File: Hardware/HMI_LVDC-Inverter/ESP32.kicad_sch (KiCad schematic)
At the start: 36 parts, among them U2 ESP32-WROOM-32E-N16, Y2 32.768KHz

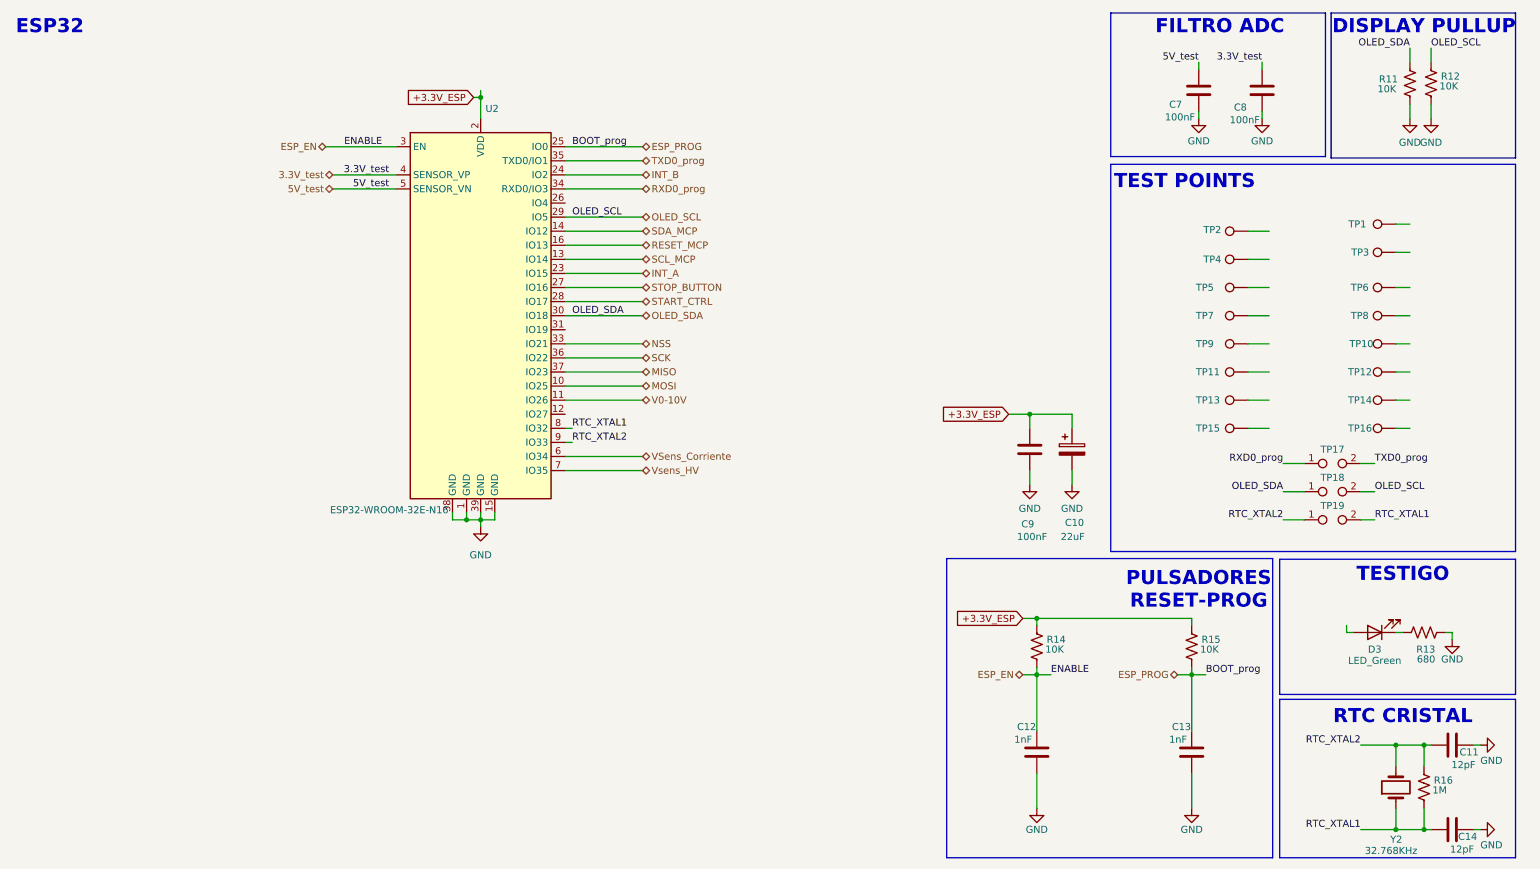
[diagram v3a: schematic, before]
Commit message: Falta resolver los pulsadores
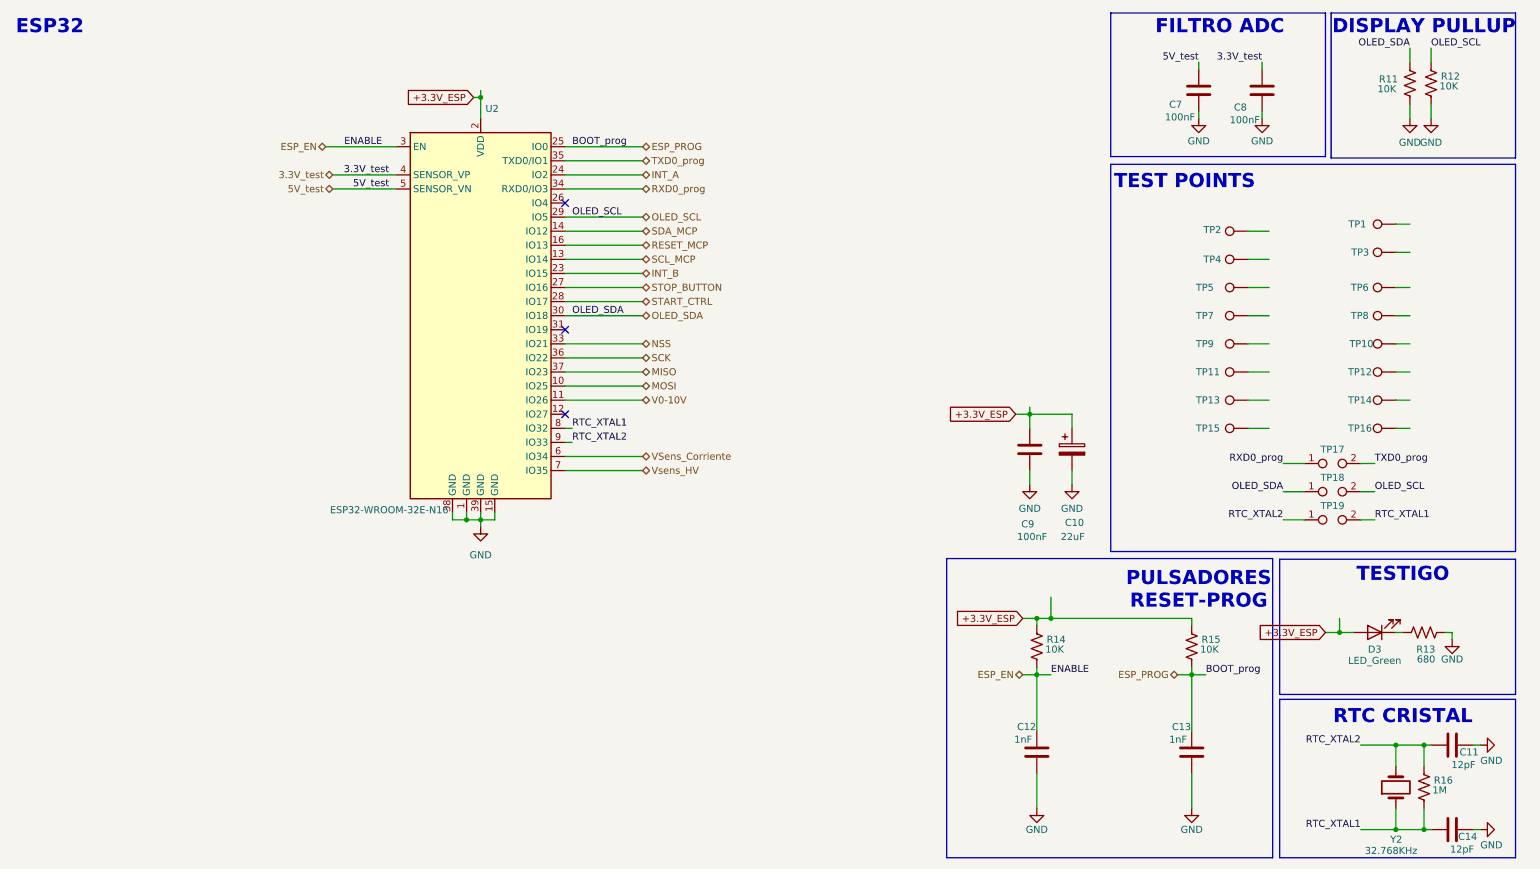
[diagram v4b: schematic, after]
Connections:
- net +3.3V_ESP: now also D3.2 (A)
- net INT_A: now also U2.24 (IO2); no longer U2.23 (IO15)
- net INT_B: now also U2.23 (IO15); no longer U2.24 (IO2)
- no-connect marks 0 -> 3

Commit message: Agregado y corrección de borneras
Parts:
- removed TP17, TP18, TP19: TestPoint_2Pole, symbol Connector:TestPoint_2Pole
- TP1, TP10, TP11, TP12, TP13, TP14, TP15, TP16, TP2, TP3, TP4, TP5, TP6, TP7, TP8, TP9: footprint Connector_Pin:Pin_D0.7mm_L6.5mm_W1.8mm_FlatFork -> TestPoint:TestPoint_Pad_D1.0mm
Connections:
- net OLED_SCL: now also TP16.1
- net OLED_SDA: now also TP15.1

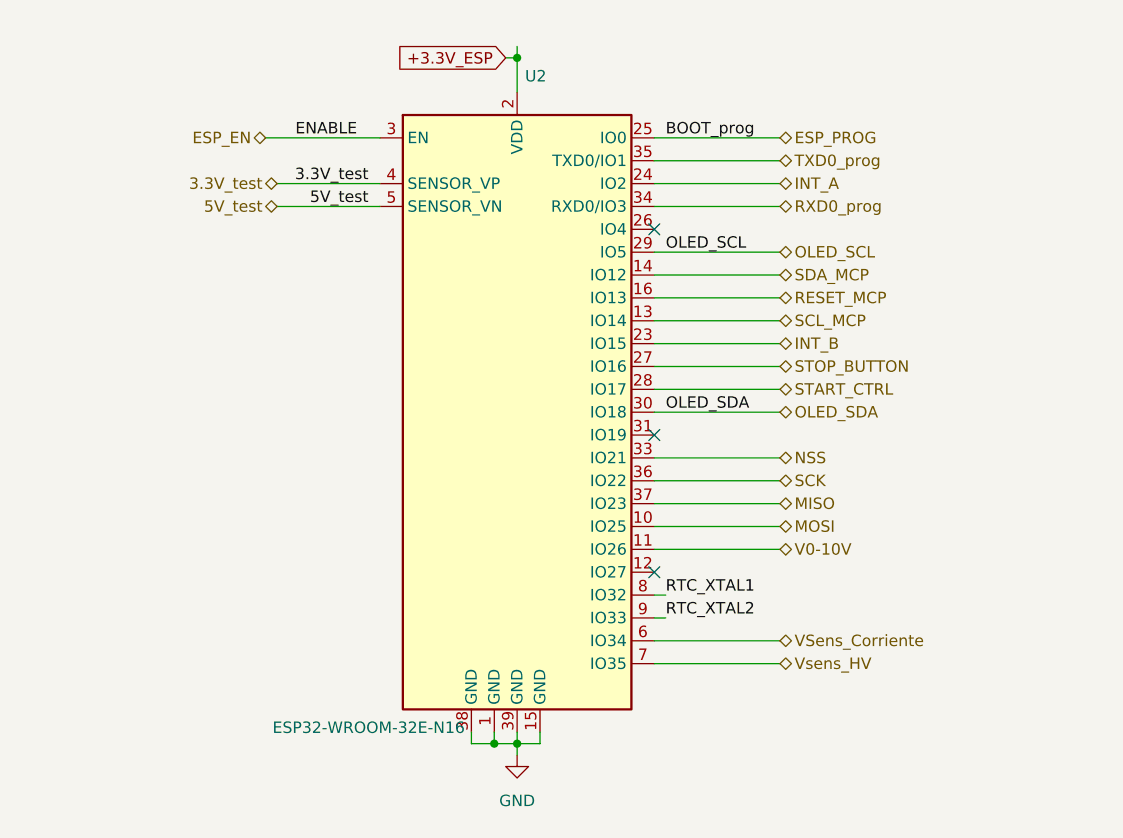
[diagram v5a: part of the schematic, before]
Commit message: Terminada la placa del HMI con revisión de reglas de diseño
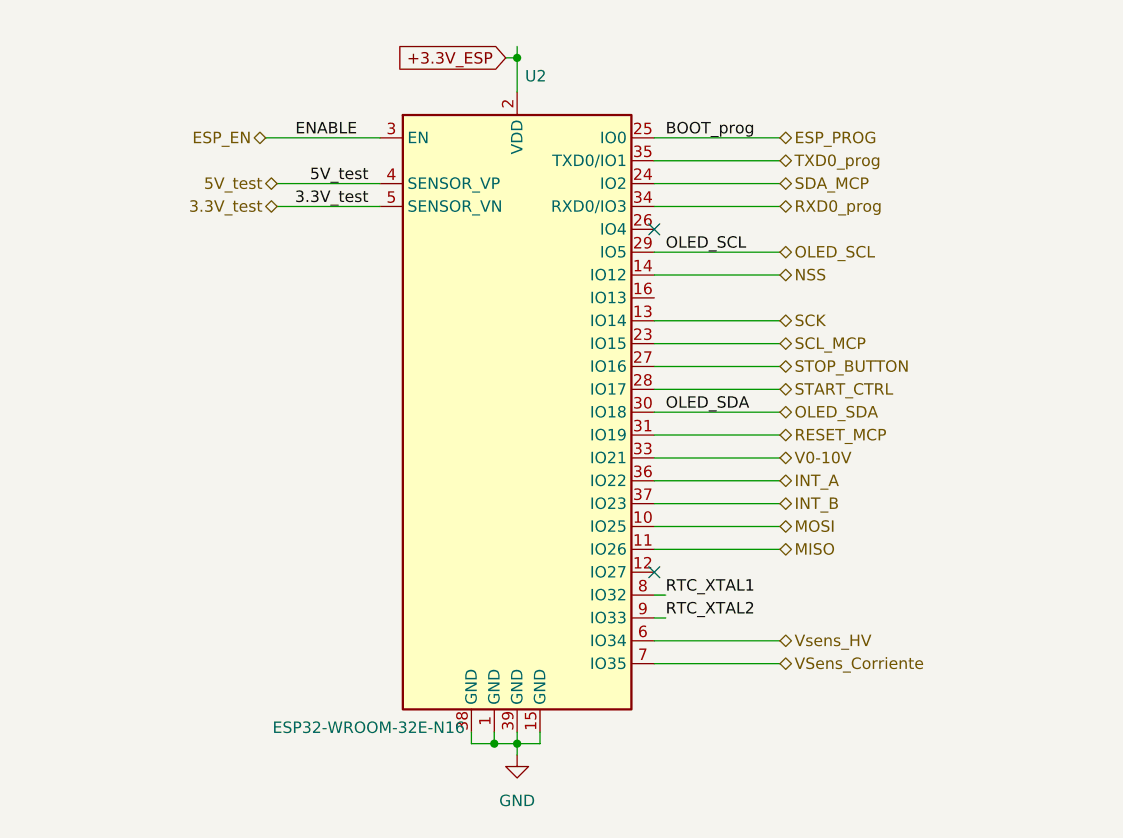
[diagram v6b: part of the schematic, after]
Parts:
- U2: footprint RF_Module:ESP32-WROOM-32D -> RF_Module:ESP32-WROOM-32E
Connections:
- net 3.3V_test: now also U2.5 (SENSOR_VN); no longer U2.4 (SENSOR_VP)
- net 5V_test: now also U2.4 (SENSOR_VP); no longer U2.5 (SENSOR_VN)
- net INT_A: now also U2.36 (IO22); no longer U2.24 (IO2)
- net INT_B: now also U2.37 (IO23); no longer U2.23 (IO15)
- net MISO: now also U2.11 (IO26); no longer U2.37 (IO23)
- net NSS: now also U2.14 (IO12); no longer U2.33 (IO21)
- net RESET_MCP: now also U2.31 (IO19); no longer U2.16 (IO13)
- net SCK: now also U2.13 (IO14); no longer U2.36 (IO22)
- net SCL_MCP: now also U2.23 (IO15); no longer U2.13 (IO14)
- net SDA_MCP: now also U2.24 (IO2); no longer U2.14 (IO12)
- net V0-10V: now also U2.33 (IO21); no longer U2.11 (IO26)
- net VSens_Corriente: now also U2.7 (IO35); no longer U2.6 (IO34)
- net Vsens_HV: now also U2.6 (IO34); no longer U2.7 (IO35)
- no-connect marks 3 -> 2
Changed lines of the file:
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@@
 	)
 	(no_connect
-		(at 111.76 69.85)
-	)
-	(no_connect
 		(at 111.76 46.99)
 	)
@@
 	(wire
 		(pts
-			(xy 125.73 74.93) (xy 111.76 74.93)
+			(xy 238.76 87.63) (xy 234.95 87.63)
 		)
 		(stroke
@@
 	(wire
 		(pts
-			(xy 238.76 87.63) (xy 234.95 87.63)
+			(xy 125.73 72.39) (xy 111.76 72.39)
 		)
 		(stroke
@@
 	(wire
 		(pts
-			(xy 125.73 77.47) (xy 111.76 77.47)
+			(xy 111.76 92.71) (xy 125.73 92.71)
 		)
 		(stroke
@@
 	(wire
 		(pts
-			(xy 125.73 52.07) (xy 111.76 52.07)
+			(xy 125.73 77.47) (xy 111.76 77.47)
 		)
 		(stroke
@@
 	(wire
 		(pts
-			(xy 125.73 54.61) (xy 111.76 54.61)
+			(xy 69.85 41.91) (xy 81.28 41.91)
 		)
 		(stroke
@@
 	(wire
 		(pts
-			(xy 125.73 41.91) (xy 111.76 41.91)
+			(xy 261.62 144.78) (xy 266.7 144.78)
 		)
 		(stroke
@@
 	(wire
 		(pts
-			(xy 261.62 144.78) (xy 266.7 144.78)
+			(xy 111.76 82.55) (xy 125.73 82.55)
 		)
 		(stroke
@@
 	(wire
 		(pts
-			(xy 111.76 67.31) (xy 125.73 67.31)
+			(xy 125.73 74.93) (xy 111.76 74.93)
 		)
 		(stroke
@@
 	(wire
 		(pts
-			(xy 264.16 62.23) (xy 261.62 62.23)
+			(xy 111.76 67.31) (xy 125.73 67.31)
 		)
 		(stroke
@@
 	(wire
 		(pts
-			(xy 125.73 80.01) (xy 111.76 80.01)
+			(xy 264.16 62.23) (xy 261.62 62.23)
 		)
 		(stroke
@@
 	(wire
 		(pts
-			(xy 224.79 149.86) (xy 224.79 156.21)
+			(xy 125.73 80.01) (xy 111.76 80.01)
 		)
 		(stroke
@@
 	(wire
 		(pts
-			(xy 238.76 82.55) (xy 234.95 82.55)
+			(xy 224.79 149.86) (xy 224.79 156.21)
 		)
 		(stroke
@@
 	(wire
 		(pts
-			(xy 266.7 144.78) (xy 266.7 148.59)
+			(xy 238.76 82.55) (xy 234.95 82.55)
 		)
 		(stroke
@@
 	(wire
 		(pts
-			(xy 111.76 49.53) (xy 125.73 49.53)
+			(xy 266.7 144.78) (xy 266.7 148.59)
 		)
 		(stroke
@@
 	(wire
 		(pts
-			(xy 125.73 95.25) (xy 111.76 95.25)
+			(xy 111.76 49.53) (xy 125.73 49.53)
 		)
 		(stroke
@@
 	(wire
 		(pts
-			(xy 69.85 44.45) (xy 81.28 44.45)
-		)
-		(stroke
-			(width 0)
-			(type default)
-		)
-	)
-	(wire
-		(pts
 			(xy 255.27 160.02) (xy 261.62 160.02)
 		)
@@
 	(wire
 		(pts
-			(xy 125.73 59.69) (xy 111.76 59.69)
+			(xy 125.73 69.85) (xy 111.76 69.85)
 		)
 		(stroke
@@
 	(wire
 		(pts
-			(xy 125.73 82.55) (xy 111.76 82.55)
-		)
-		(stroke
-			(width 0)
-			(type default)
-		)
-	)
-	(wire
-		(pts
 			(xy 226.06 31.75) (xy 226.06 30.48)
 		)
@@
 	(wire
 		(pts
-			(xy 195.58 85.09) (xy 203.2 85.09)
+			(xy 125.73 59.69) (xy 111.76 59.69)
 		)
 		(stroke
@@
 	(wire
 		(pts
-			(xy 203.2 95.25) (xy 203.2 97.79)
+			(xy 125.73 41.91) (xy 111.76 41.91)
 		)
 		(stroke
@@
 	(wire
 		(pts
-			(xy 261.62 156.21) (xy 261.62 160.02)
+			(xy 195.58 85.09) (xy 203.2 85.09)
 		)
 		(stroke
@@
 	(wire
 		(pts
-			(xy 238.76 72.39) (xy 234.95 72.39)
+			(xy 203.2 95.25) (xy 203.2 97.79)
 		)
 		(stroke
@@
 	(wire
 		(pts
-			(xy 248.92 124.46) (xy 251.46 124.46)
+			(xy 261.62 156.21) (xy 261.62 160.02)
 		)
 		(stroke
@@
 	(wire
 		(pts
-			(xy 125.73 57.15) (xy 111.76 57.15)
+			(xy 238.76 72.39) (xy 234.95 72.39)
 		)
 		(stroke
@@
 	(wire
 		(pts
-			(xy 96.52 26.67) (xy 96.52 27.94)
+			(xy 248.92 124.46) (xy 251.46 124.46)
 		)
 		(stroke
@@
 	(wire
 		(pts
-			(xy 224.79 132.08) (xy 224.79 142.24)
+			(xy 96.52 26.67) (xy 96.52 27.94)
 		)
 		(stroke
@@
 	(wire
 		(pts
-			(xy 125.73 92.71) (xy 111.76 92.71)
+			(xy 224.79 132.08) (xy 224.79 142.24)
 		)
 		(stroke
@@
 	(wire
 		(pts
-			(xy 125.73 72.39) (xy 111.76 72.39)
+			(xy 238.76 67.31) (xy 234.95 67.31)
 		)
 		(stroke
@@
 	(wire
 		(pts
-			(xy 238.76 67.31) (xy 234.95 67.31)
+			(xy 196.85 121.92) (xy 196.85 123.19)
 		)
 		(stroke
@@
 	(wire
 		(pts
-			(xy 196.85 121.92) (xy 196.85 123.19)
+			(xy 264.16 31.75) (xy 264.16 29.21)
 		)
 		(stroke
@@
 	(wire
 		(pts
-			(xy 264.16 31.75) (xy 264.16 29.21)
+			(xy 264.16 72.39) (xy 261.62 72.39)
 		)
 		(stroke
@@
 	(wire
 		(pts
-			(xy 264.16 72.39) (xy 261.62 72.39)
+			(xy 111.76 95.25) (xy 125.73 95.25)
+		)
+		(stroke
+			(width 0)
+			(type default)
+		)
+	)
+	(wire
+		(pts
+			(xy 111.76 57.15) (xy 125.73 57.15)
 		)
 		(stroke
@@
 	(wire
 		(pts
-			(xy 69.85 41.91) (xy 81.28 41.91)
+			(xy 111.76 52.07) (xy 125.73 52.07)
+		)
+		(stroke
+			(width 0)
+			(type default)
+		)
+	)
+	(wire
+		(pts
+			(xy 69.85 44.45) (xy 81.28 44.45)
 		)
 		(stroke
@@
 		)
 	)
-	(label "5V_test"
-		(at 80.01 44.45 180)
-		(effects
-			(font
-				(size 1.27 1.27)
-			)
-			(justify right bottom)
-		)
-	)
 	(label "OLED_SDA"
 		(at 238.76 87.63 0)
@@
 		)
 	)
+	(label "5V_test"
+		(at 80.01 41.91 180)
+		(effects
+			(font
+				(size 1.27 1.27)
+			)
+			(justify right bottom)
+		)
+	)
 	(label "ENABLE"
 		(at 199.39 132.08 0)
@@
 	)
 	(label "3.3V_test"
-		(at 80.01 41.91 180)
+		(at 80.01 44.45 180)
 		(effects
 			(font
@@
 	(hierarchical_label "SCL_MCP"
 		(shape bidirectional)
-		(at 125.73 57.15 0)
+		(at 125.73 59.69 0)
 		(effects
 			(font
@@
 	(hierarchical_label "INT_A"
 		(shape bidirectional)
-		(at 125.73 41.91 0)
+		(at 125.73 74.93 0)
 		(effects
 			(font
@@
 	(hierarchical_label "V0-10V"
 		(shape bidirectional)
-		(at 125.73 82.55 0)
+		(at 125.73 72.39 0)
 		(effects
 			(font
@@
 		)
 	)
+	(hierarchical_label "5V_test"
+		(shape bidirectional)
+		(at 69.85 41.91 180)
+		(effects
+			(font
+				(size 1.27 1.27)
+			)
+			(justify right)
+		)
+	)
 	(hierarchical_label "RESET_MCP"
 		(shape bidirectional)
-		(at 125.73 54.61 0)
+		(at 125.73 69.85 0)
 		(effects
 			(font
@@
 	(hierarchical_label "NSS"
 		(shape bidirectional)
-		(at 125.73 72.39 0)
+		(at 125.73 52.07 0)
 		(effects
 			(font
@@
 	(hierarchical_label "VSens_Corriente"
 		(shape bidirectional)
-		(at 125.73 92.71 0)
+		(at 125.73 95.25 0)
 		(effects
 			(font
@@
 		)
 	)
-	(hierarchical_label "5V_test"
-		(shape bidirectional)
-		(at 69.85 44.45 180)
-		(effects
-			(font
-				(size 1.27 1.27)
-			)
-			(justify right)
-		)
-	)
 	(hierarchical_label "ESP_PROG"
 		(shape bidirectional)
@@
 	(hierarchical_label "MISO"
 		(shape bidirectional)
-		(at 125.73 77.47 0)
+		(at 125.73 82.55 0)
 		(effects
 			(font
@@
 	(hierarchical_label "SCK"
 		(shape bidirectional)
-		(at 125.73 74.93 0)
+		(at 125.73 57.15 0)
 		(effects
 			(font
@@
 	(hierarchical_label "Vsens_HV"
 		(shape bidirectional)
-		(at 125.73 95.25 0)
+		(at 125.73 92.71 0)
 		(effects
 			(font
@@
 	(hierarchical_label "INT_B"
 		(shape bidirectional)
-		(at 125.73 59.69 0)
+		(at 125.73 77.47 0)
 		(effects
 			(font
@@
 	(hierarchical_label "3.3V_test"
 		(shape bidirectional)
-		(at 69.85 41.91 180)
+		(at 69.85 44.45 180)
 		(effects
 			(font
@@
 	(hierarchical_label "SDA_MCP"
 		(shape bidirectional)
-		(at 125.73 52.07 0)
+		(at 125.73 41.91 0)
 		(effects
 			(font
@@
 		(at 261.62 152.4 90)
 		(unit 1)
-		(exclude_from_sim no)
+		(exclude_from_sim yes)
 		(in_bom yes)
 		(on_board yes)
@@
 			)
 		)
-		(property "Footprint" "RF_Module:ESP32-WROOM-32D"
+		(property "Footprint" "RF_Module:ESP32-WROOM-32E"
 			(at 113.03 101.6 0)
 			(effects

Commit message: Cambio de pin de 0-10V
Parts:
- removed TP1, TP10, TP11, TP12, TP13, TP14, TP15, TP16, TP2, TP3, TP4, TP5, TP6, TP7, TP8, TP9: TestPoint, TestPoint:TestPoint_Pad_D1.0mm, symbol Connector:TestPoint
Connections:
- net V0-10V: now also U2.26 (IO4); no longer U2.33 (IO21)
- no-connect marks 2 -> 3
